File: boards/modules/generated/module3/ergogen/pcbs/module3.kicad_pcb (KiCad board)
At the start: 2 copper layers, 75.2 x 75.2 mm, 13 parts

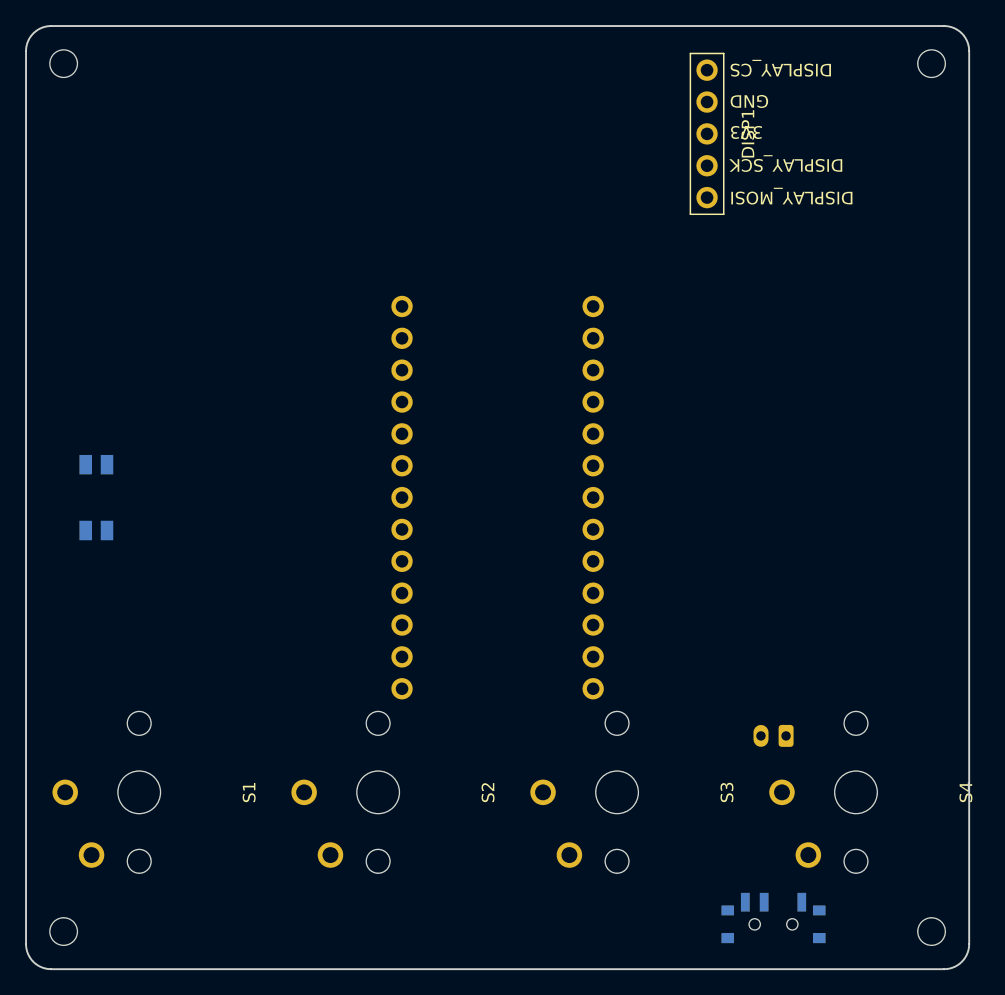
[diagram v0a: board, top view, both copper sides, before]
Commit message: Route every module with broad ground planes and retain TPS43 with top display
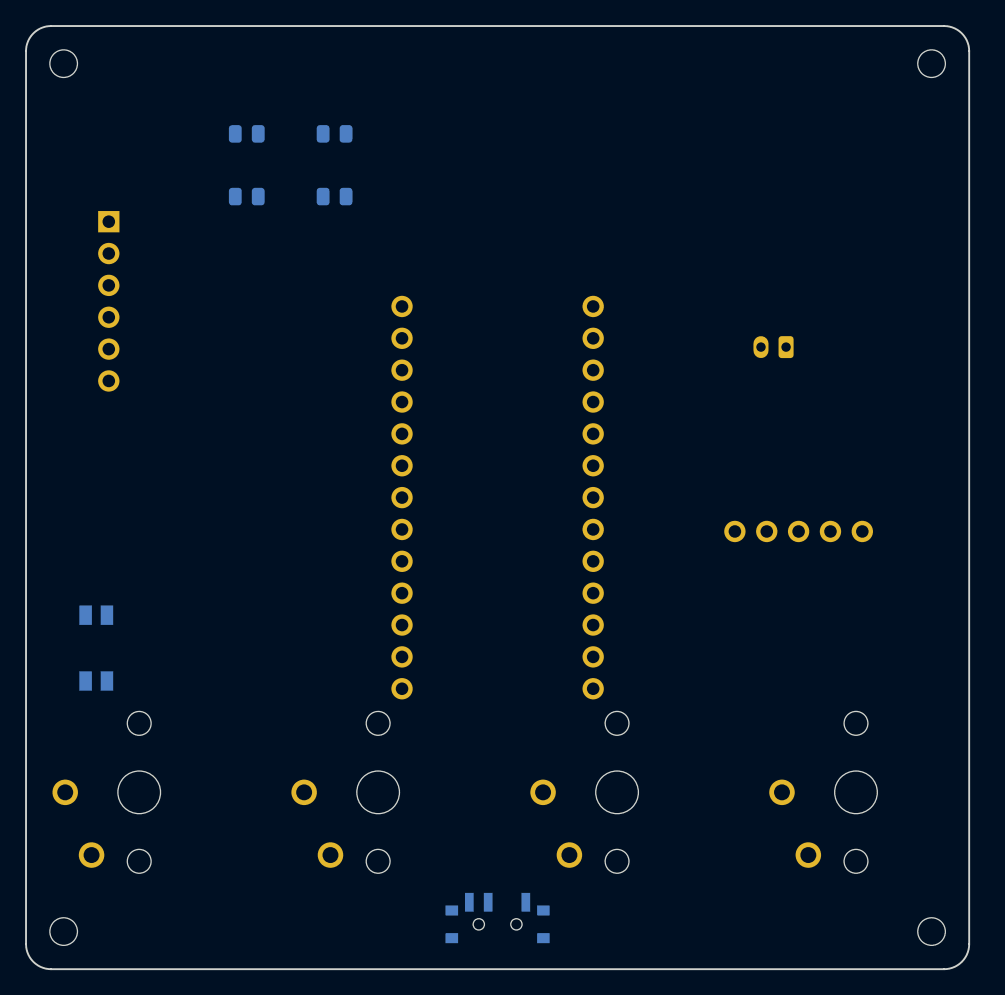
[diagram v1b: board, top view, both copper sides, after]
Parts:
- added R1: 4.7k, R_0805_2012Metric, B.Cu at (80.0, 71.0)
- added R2: 4.7k, R_0805_2012Metric, B.Cu at (80.0, 76.0)
- added R3: 10k, R_0805_2012Metric, B.Cu at (87.0, 71.0)
- added R4: 10k, R_0805_2012Metric, B.Cu at (87.0, 76.0)
- added TP1: TPS43 cable adapter, TPS43_Cable_Header_1x06_P2.54, B.Cu at (69.0, 78.0)
- DISP1: footprint ceoloide:display_nice_view -> display_nice_view
- JST1: footprint ceoloide:battery_connector_jst_ph_2 -> battery_connector_jst_ph_2
- MCU1: footprint ceoloide:mcu_nice_nano -> mcu_nice_nano
- MH1, MH2, MH3, MH4: footprint ceoloide:mounting_hole_npth -> mounting_hole_npth
- PWR1: footprint ceoloide:power_switch_smd_side -> power_switch_smd_side
- RST1: footprint ceoloide:reset_switch_smd_side -> reset_switch_smd_side
- S1, S2, S3, S4: footprint ceoloide:switch_choc_v1_v2 -> switch_choc_v1_v2
- moved JST1 31.0 mm to (122.0, 88.0)
- moved DISP1 28.3 mm to (124.0, 86.0), turned to 0 degrees
- moved PWR1 22.0 mm to (100.0, 134.0)
- moved RST1 12.0 mm to (68.0, 112.0)
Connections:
- MCU1 pad 10: P14 -> TP_SDA
- MCU1 pad 11: P16 -> TP_RDY
- MCU1 pad 8: P18 -> TP_RST
- MCU1 pad 9: P15 -> TP_SCL
